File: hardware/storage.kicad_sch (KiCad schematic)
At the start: 15 parts, among them J6 Micro_SD_Card_Det1, U21 EMMC5.1_BGA153

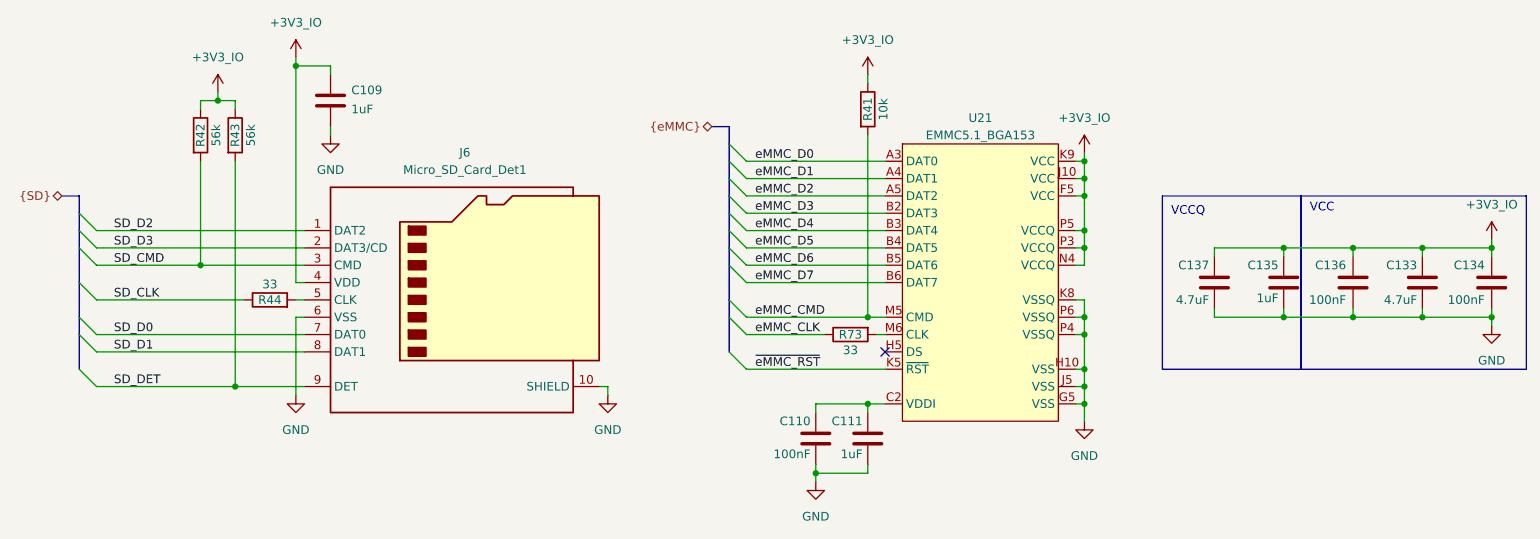
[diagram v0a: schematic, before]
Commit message: Update crystal
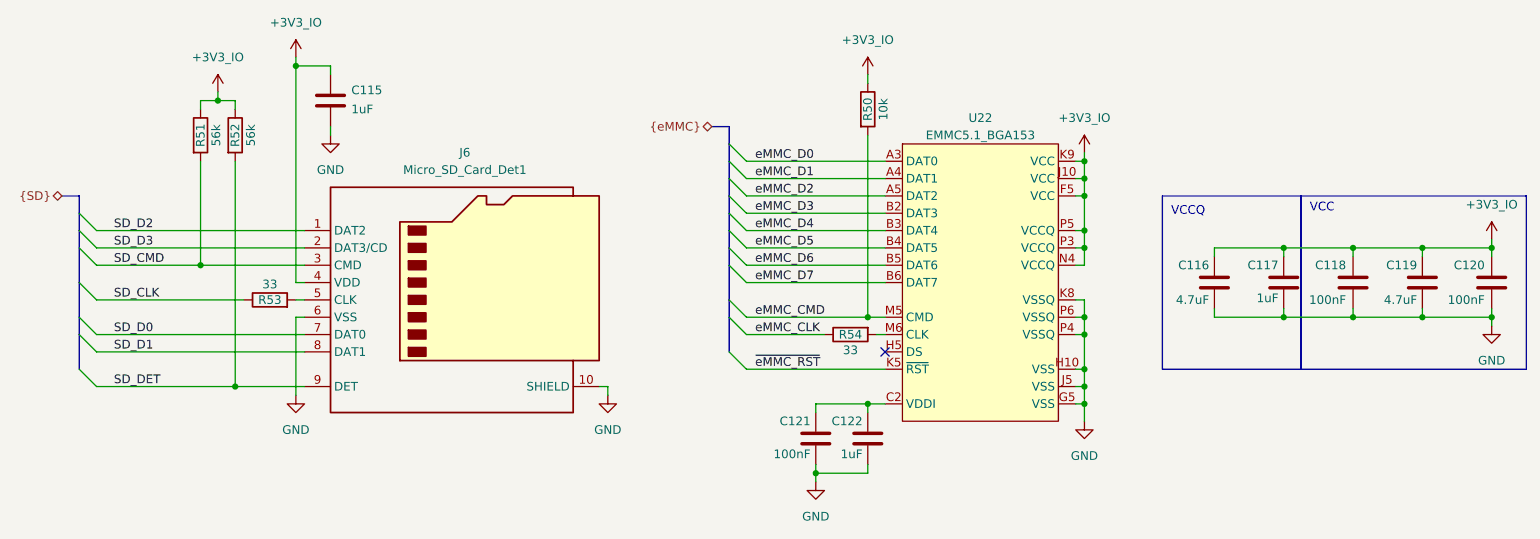
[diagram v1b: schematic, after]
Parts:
- renumbered C109 to C115, C137 to C116, C135 to C117, C136 to C118, C133 to C119, C134 to C120, C110 to C121, C111 to C122, R41 to R50, R42 to R51, R43 to R52, R44 to R53, R73 to R54, U21 to U22
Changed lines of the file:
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@@
 		(dnp no)
 		(fields_autoplaced yes)
-		(property "Reference" "#PWR0131"
+		(property "Reference" "#PWR0151"
 			(at 85.09 72.39 0)
 			(effects
@@
 			(project "cm0"
 				(path "/b53f5dbb-8078-4818-9e8f-fdf90ba6d854/bbbf0a3c-34ab-4b2d-85d9-faf7e9a88445"
-					(reference "#PWR0131")
+					(reference "#PWR0151")
 					(unit 1)
 				)
@@
 		(dnp no)
 		(fields_autoplaced yes)
-		(property "Reference" "#PWR0132"
+		(property "Reference" "#PWR0152"
 			(at 101.6 81.28 0)
 			(effects
@@
 			(project "cm0"
 				(path "/b53f5dbb-8078-4818-9e8f-fdf90ba6d854/bbbf0a3c-34ab-4b2d-85d9-faf7e9a88445"
-					(reference "#PWR0132")
+					(reference "#PWR0152")
 					(unit 1)
 				)
@@
 		(on_board yes)
 		(dnp no)
-		(property "Reference" "C111"
+		(property "Reference" "C122"
 			(at 179.578 116.84 0)
 			(effects
@@
 			(project "cm0"
 				(path "/b53f5dbb-8078-4818-9e8f-fdf90ba6d854/bbbf0a3c-34ab-4b2d-85d9-faf7e9a88445"
-					(reference "C111")
+					(reference "C122")
 					(unit 1)
 				)
@@
 		(on_board yes)
 		(dnp no)
-		(property "Reference" "R41"
+		(property "Reference" "R50"
 			(at 180.34 71.12 90)
 			(effects
@@
 			(project "cm0"
 				(path "/b53f5dbb-8078-4818-9e8f-fdf90ba6d854/bbbf0a3c-34ab-4b2d-85d9-faf7e9a88445"
-					(reference "R41")
+					(reference "R50")
 					(unit 1)
 				)
@@
 		(on_board yes)
 		(dnp no)
-		(property "Reference" "R42"
+		(property "Reference" "R51"
 			(at 82.55 74.93 90)
 			(effects
@@
 			(project "cm0"
 				(path "/b53f5dbb-8078-4818-9e8f-fdf90ba6d854/bbbf0a3c-34ab-4b2d-85d9-faf7e9a88445"
-					(reference "R42")
+					(reference "R51")
 					(unit 1)
 				)
@@
 		(on_board yes)
 		(dnp no)
-		(property "Reference" "C110"
+		(property "Reference" "C121"
 			(at 171.958 116.84 0)
 			(effects
@@
 			(project "cm0"
 				(path "/b53f5dbb-8078-4818-9e8f-fdf90ba6d854/bbbf0a3c-34ab-4b2d-85d9-faf7e9a88445"
-					(reference "C110")
+					(reference "C121")
 					(unit 1)
 				)
@@
 		(dnp no)
 		(fields_autoplaced yes)
-		(property "Reference" "#PWR0135"
+		(property "Reference" "#PWR0157"
 			(at 142.24 119.38 0)
 			(effects
@@
 			(project ""
 				(path "/b53f5dbb-8078-4818-9e8f-fdf90ba6d854/bbbf0a3c-34ab-4b2d-85d9-faf7e9a88445"
-					(reference "#PWR0135")
+					(reference "#PWR0157")
 					(unit 1)
 				)
@@
 		(on_board yes)
 		(dnp no)
-		(property "Reference" "C136"
+		(property "Reference" "C118"
 			(at 250.444 93.98 0)
 			(effects
@@
 			(project "cm0"
 				(path "/b53f5dbb-8078-4818-9e8f-fdf90ba6d854/bbbf0a3c-34ab-4b2d-85d9-faf7e9a88445"
-					(reference "C136")
+					(reference "C118")
 					(unit 1)
 				)
@@
 		(on_board yes)
 		(dnp no)
-		(property "Reference" "C134"
+		(property "Reference" "C120"
 			(at 270.764 93.98 0)
 			(effects
@@
 			(project "cm0"
 				(path "/b53f5dbb-8078-4818-9e8f-fdf90ba6d854/bbbf0a3c-34ab-4b2d-85d9-faf7e9a88445"
-					(reference "C134")
+					(reference "C120")
 					(unit 1)
 				)
@@
 		(dnp no)
 		(fields_autoplaced yes)
-		(property "Reference" "#PWR0134"
+		(property "Reference" "#PWR0156"
 			(at 96.52 119.38 0)
 			(effects
@@
 			(project ""
 				(path "/b53f5dbb-8078-4818-9e8f-fdf90ba6d854/bbbf0a3c-34ab-4b2d-85d9-faf7e9a88445"
-					(reference "#PWR0134")
+					(reference "#PWR0156")
 					(unit 1)
 				)
@@
 		(on_board yes)
 		(dnp no)
-		(property "Reference" "C137"
+		(property "Reference" "C116"
 			(at 230.378 93.98 0)
 			(effects
@@
 			(project "cm0"
 				(path "/b53f5dbb-8078-4818-9e8f-fdf90ba6d854/bbbf0a3c-34ab-4b2d-85d9-faf7e9a88445"
-					(reference "C137")
+					(reference "C116")
 					(unit 1)
 				)
@@
 		(dnp no)
 		(fields_autoplaced yes)
-		(property "Reference" "#PWR0129"
+		(property "Reference" "#PWR0149"
 			(at 96.52 67.31 0)
 			(effects
@@
 			(project ""
 				(path "/b53f5dbb-8078-4818-9e8f-fdf90ba6d854/bbbf0a3c-34ab-4b2d-85d9-faf7e9a88445"
-					(reference "#PWR0129")
+					(reference "#PWR0149")
 					(unit 1)
 				)
@@
 		(on_board yes)
 		(dnp no)
-		(property "Reference" "C135"
+		(property "Reference" "C117"
 			(at 240.538 93.98 0)
 			(effects
@@
 			(project "cm0"
 				(path "/b53f5dbb-8078-4818-9e8f-fdf90ba6d854/bbbf0a3c-34ab-4b2d-85d9-faf7e9a88445"
-					(reference "C135")
+					(reference "C117")
 					(unit 1)
 				)
@@
 		(on_board yes)
 		(dnp no)
-		(property "Reference" "R44"
+		(property "Reference" "R53"
 			(at 92.71 99.06 90)
 			(effects
@@
 			(project "cm0"
 				(path "/b53f5dbb-8078-4818-9e8f-fdf90ba6d854/bbbf0a3c-34ab-4b2d-85d9-faf7e9a88445"
-					(reference "R44")
+					(reference "R53")
 					(unit 1)
 				)
@@
 		(on_board yes)
 		(dnp no)
-		(property "Reference" "C133"
+		(property "Reference" "C119"
 			(at 260.858 93.98 0)
 			(effects
@@
 			(project "cm0"
 				(path "/b53f5dbb-8078-4818-9e8f-fdf90ba6d854/bbbf0a3c-34ab-4b2d-85d9-faf7e9a88445"
-					(reference "C133")
+					(reference "C119")
 					(unit 1)
 				)
@@
 		(dnp no)
 		(fields_autoplaced yes)
-		(property "Reference" "#PWR0187"
+		(property "Reference" "#PWR0154"
 			(at 271.78 93.98 0)
 			(effects
@@
 			(project "cm0"
 				(path "/b53f5dbb-8078-4818-9e8f-fdf90ba6d854/bbbf0a3c-34ab-4b2d-85d9-faf7e9a88445"
-					(reference "#PWR0187")
+					(reference "#PWR0154")
 					(unit 1)
 				)
@@
 		(dnp no)
 		(fields_autoplaced yes)
-		(property "Reference" "#PWR0136"
+		(property "Reference" "#PWR0158"
 			(at 212.09 123.19 0)
 			(effects
@@
 			(project "cm0"
 				(path "/b53f5dbb-8078-4818-9e8f-fdf90ba6d854/bbbf0a3c-34ab-4b2d-85d9-faf7e9a88445"
-					(reference "#PWR0136")
+					(reference "#PWR0158")
 					(unit 1)
 				)
@@
 		(dnp no)
 		(fields_autoplaced yes)
-		(property "Reference" "#PWR0176"
+		(property "Reference" "#PWR0153"
 			(at 212.09 81.28 0)
 			(effects
@@
 			(project "cm0"
 				(path "/b53f5dbb-8078-4818-9e8f-fdf90ba6d854/bbbf0a3c-34ab-4b2d-85d9-faf7e9a88445"
-					(reference "#PWR0176")
+					(reference "#PWR0153")
 					(unit 1)
 				)
@@
 		(dnp no)
 		(fields_autoplaced yes)
-		(property "Reference" "#PWR0137"
+		(property "Reference" "#PWR0159"
 			(at 172.72 132.08 0)
 			(effects
@@
 			(project ""
 				(path "/b53f5dbb-8078-4818-9e8f-fdf90ba6d854/bbbf0a3c-34ab-4b2d-85d9-faf7e9a88445"
-					(reference "#PWR0137")
+					(reference "#PWR0159")
 					(unit 1)
 				)
@@
 		(on_board yes)
 		(dnp no)
-		(property "Reference" "R43"
+		(property "Reference" "R52"
 			(at 87.63 74.93 90)
 			(effects
@@
 			(project "cm0"
 				(path "/b53f5dbb-8078-4818-9e8f-fdf90ba6d854/bbbf0a3c-34ab-4b2d-85d9-faf7e9a88445"
-					(reference "R43")
+					(reference "R52")
 					(unit 1)
 				)
@@
 		(dnp no)
 		(fields_autoplaced yes)
-		(property "Reference" "#PWR0130"
+		(property "Reference" "#PWR0150"
 			(at 180.34 69.85 0)
 			(effects
@@
 			(project "cm0"
 				(path "/b53f5dbb-8078-4818-9e8f-fdf90ba6d854/bbbf0a3c-34ab-4b2d-85d9-faf7e9a88445"
-					(reference "#PWR0130")
+					(reference "#PWR0150")
 					(unit 1)
 				)
@@
 		(dnp no)
 		(fields_autoplaced yes)
-		(property "Reference" "#PWR0186"
+		(property "Reference" "#PWR0155"
 			(at 271.78 109.22 0)
 			(effects
@@
 			(project "cm0"
 				(path "/b53f5dbb-8078-4818-9e8f-fdf90ba6d854/bbbf0a3c-34ab-4b2d-85d9-faf7e9a88445"
-					(reference "#PWR0186")
+					(reference "#PWR0155")
 					(unit 1)
 				)
@@
 		(dnp no)
 		(fields_autoplaced yes)
-		(property "Reference" "U21"
+		(property "Reference" "U22"
 			(at 196.85 72.39 0)
 			(effects
@@
 			(project ""
 				(path "/b53f5dbb-8078-4818-9e8f-fdf90ba6d854/bbbf0a3c-34ab-4b2d-85d9-faf7e9a88445"
-					(reference "U21")
+					(reference "U22")
 					(unit 1)
 				)
@@
 		(on_board yes)
 		(dnp no)
-		(property "Reference" "R73"
+		(property "Reference" "R54"
 			(at 177.8 104.14 90)
 			(effects
@@
 			(project "cm0"
 				(path "/b53f5dbb-8078-4818-9e8f-fdf90ba6d854/bbbf0a3c-34ab-4b2d-85d9-faf7e9a88445"
-					(reference "R73")
+					(reference "R54")
 					(unit 1)
 				)
@@
 		(on_board yes)
 		(dnp no)
-		(property "Reference" "C109"
+		(property "Reference" "C115"
 			(at 104.648 68.326 0)
 			(effects
@@
 			(project "cm0"
 				(path "/b53f5dbb-8078-4818-9e8f-fdf90ba6d854/bbbf0a3c-34ab-4b2d-85d9-faf7e9a88445"
-					(reference "C109")
-					(unit 1)
-				)
+					(reference "C115")
+					(unit 1)
+				)

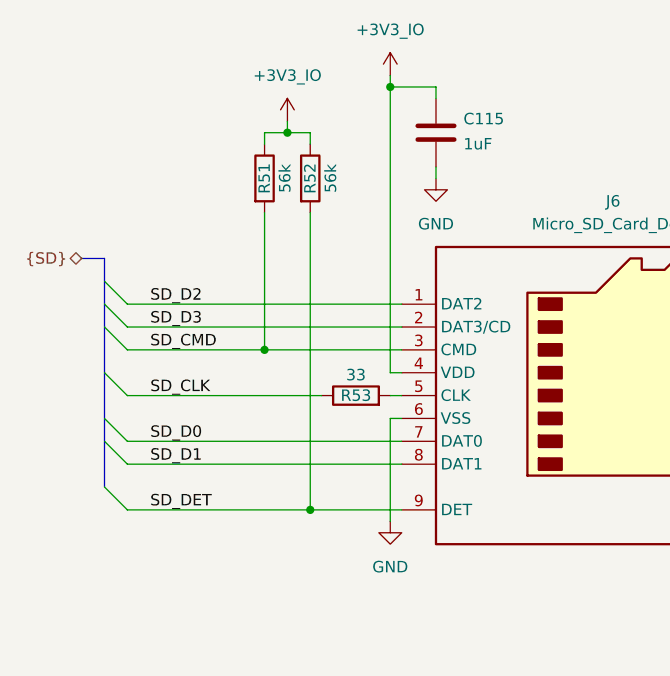
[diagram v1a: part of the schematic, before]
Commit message: Add schematic pdf
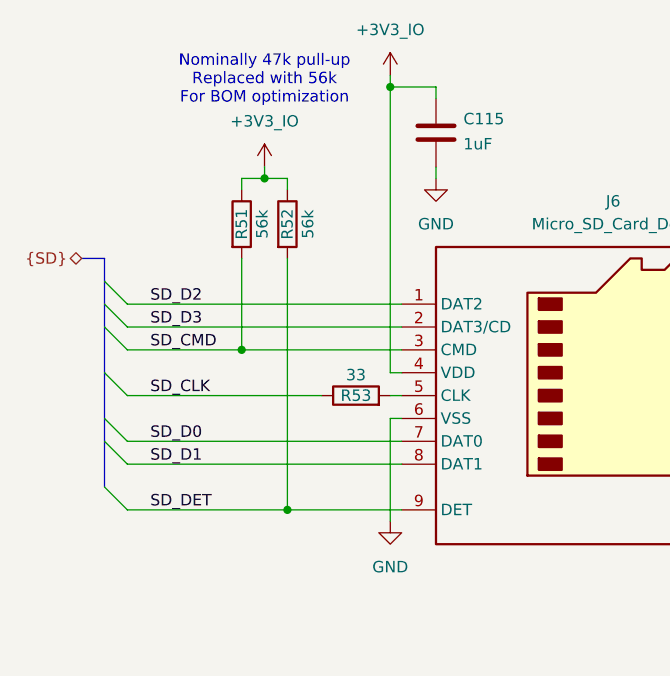
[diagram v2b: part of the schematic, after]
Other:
- note added: "Nominally 47k pull-up Replaced with 56k For BOM optimization"
- title: Icepi CM0 -> Icepi SBC
- moved on the sheet: R51, R52
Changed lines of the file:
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@@
 	(paper "A4")
 	(title_block
-		(title "Icepi CM0")
-		(date "2025-11-21")
+		(title "Icepi SBC")
+		(date "2025-12-21")
 		(rev "v1.0")
 		(company "Icy Electronics")
 		(comment 1 "Chengyin Yao (cheyao)")
-		(comment 2 "https://github.com/cheyao/icepi-cm0")
+		(comment 2 "https://github.com/cheyao/icepi-sbc")
 		(comment 3 "License: Solderpad")
 	)
@@
 		)
 	)
+	(text "Nominally 47k pull-up\nReplaced with 56k\nFor BOM optimization"
+		(exclude_from_sim no)
+		(at 82.55 64.008 0)
+		(effects
+			(font
+				(size 1.27 1.27)
+			)
+		)
+	)
 	(text "VCCQ"
 		(exclude_from_sim no)
@@
 	)
 	(junction
-		(at 87.63 111.76)
-		(diameter 0)
-		(color 0 0 0 0)
-	)
-	(junction
 		(at 251.46 91.44)
 		(diameter 0)
@@
 	)
 	(junction
+		(at 80.01 93.98)
+		(diameter 0)
+		(color 0 0 0 0)
+	)
+	(junction
 		(at 212.09 101.6)
 		(diameter 0)
@@
 	)
 	(junction
-		(at 85.09 69.85)
+		(at 82.55 74.93)
 		(diameter 0)
 		(color 0 0 0 0)
@@
 	)
 	(junction
-		(at 82.55 93.98)
-		(diameter 0)
-		(color 0 0 0 0)
-	)
-	(junction
 		(at 271.78 101.6)
 		(diameter 0)
@@
 	)
 	(junction
+		(at 85.09 111.76)
+		(diameter 0)
+		(color 0 0 0 0)
+	)
+	(junction
 		(at 271.78 91.44)
 		(diameter 0)
@@
 	(wire
 		(pts
-			(xy 85.09 68.58) (xy 85.09 69.85)
+			(xy 82.55 73.66) (xy 82.55 74.93)
 		)
 		(stroke
@@
 	(wire
 		(pts
-			(xy 87.63 111.76) (xy 97.79 111.76)
-		)
-		(stroke
-			(width 0)
-			(type default)
-		)
-	)
-	(wire
-		(pts
 			(xy 67.31 106.68) (xy 97.79 106.68)
 		)
@@
 		)
 	)
-	(wire
-		(pts
-			(xy 82.55 93.98) (xy 97.79 93.98)
-		)
-		(stroke
-			(width 0)
-			(type default)
-		)
-	)
 	(bus
 		(pts
@@
 	(wire
 		(pts
-			(xy 67.31 111.76) (xy 87.63 111.76)
+			(xy 67.31 111.76) (xy 85.09 111.76)
 		)
 		(stroke
@@
 	(wire
 		(pts
-			(xy 85.09 69.85) (xy 87.63 69.85)
+			(xy 82.55 74.93) (xy 85.09 74.93)
 		)
 		(stroke
@@
 	(wire
 		(pts
-			(xy 82.55 69.85) (xy 82.55 71.12)
+			(xy 80.01 74.93) (xy 80.01 76.2)
 		)
 		(stroke
@@
 	(wire
 		(pts
-			(xy 87.63 69.85) (xy 87.63 71.12)
+			(xy 85.09 74.93) (xy 85.09 76.2)
 		)
 		(stroke
@@
 	(wire
 		(pts
-			(xy 82.55 78.74) (xy 82.55 93.98)
+			(xy 80.01 83.82) (xy 80.01 93.98)
 		)
 		(stroke
@@
 	(wire
 		(pts
+			(xy 80.01 93.98) (xy 97.79 93.98)
+		)
+		(stroke
+			(width 0)
+			(type default)
+		)
+	)
+	(wire
+		(pts
 			(xy 67.31 99.06) (xy 88.9 99.06)
 		)
@@
 	(wire
 		(pts
-			(xy 67.31 93.98) (xy 82.55 93.98)
+			(xy 67.31 93.98) (xy 80.01 93.98)
 		)
 		(stroke
@@
 	(wire
 		(pts
-			(xy 85.09 69.85) (xy 82.55 69.85)
+			(xy 82.55 74.93) (xy 80.01 74.93)
 		)
 		(stroke
@@
 	(wire
 		(pts
-			(xy 87.63 78.74) (xy 87.63 111.76)
+			(xy 85.09 83.82) (xy 85.09 111.76)
+		)
+		(stroke
+			(width 0)
+			(type default)
+		)
+	)
+	(wire
+		(pts
+			(xy 85.09 111.76) (xy 97.79 111.76)
 		)
 		(stroke
@@
 	(symbol
 		(lib_id "cm0:+3V3_IO")
-		(at 85.09 68.58 0)
+		(at 82.55 73.66 0)
 		(unit 1)
 		(exclude_from_sim no)
@@
 		(fields_autoplaced yes)
 		(property "Reference" "#PWR0151"
-			(at 85.09 72.39 0)
+			(at 82.55 77.47 0)
 			(effects
 				(font
@@
 		)
 		(property "Value" "+3V3_IO"
-			(at 85.09 63.5 0)
+			(at 82.55 68.58 0)
 			(effects
 				(font
@@
 		)
 		(property "Footprint" ""
-			(at 85.09 68.58 0)
+			(at 82.55 73.66 0)
 			(effects
 				(font
@@
 		)
 		(property "Datasheet" ""
-			(at 85.09 68.58 0)
+			(at 82.55 73.66 0)
 			(effects
 				(font
@@
 		)
 		(property "Description" "Power symbol creates a global label with name \"+3V3_IO\""
-			(at 85.09 68.58 0)
+			(at 82.55 73.66 0)
 			(effects
 				(font
@@
 	(symbol
 		(lib_id "Device:R")
-		(at 82.55 74.93 0)
+		(at 80.01 80.01 0)
 		(unit 1)
 		(exclude_from_sim no)
@@
 		(dnp no)
 		(property "Reference" "R51"
-			(at 82.55 74.93 90)
+			(at 80.01 80.01 90)
 			(effects
 				(font
@@
 		)
 		(property "Value" "56k"
-			(at 84.836 74.93 90)
+			(at 82.296 80.01 90)
 			(effects
 				(font
@@
 		)
 		(property "Footprint" "Resistor_SMD:R_0402_1005Metric"
-			(at 80.772 74.93 90)
+			(at 78.232 80.01 90)
 			(effects
 				(font
@@
 		)
 		(property "Datasheet" "~"
-			(at 82.55 74.93 0)
+			(at 80.01 80.01 0)
 			(effects
 				(font
@@
 		)
 		(property "Description" "Resistor"
-			(at 82.55 74.93 0)
+			(at 80.01 80.01 0)
 			(effects
 				(font
@@
 		)
 		(property "LCSC Part #" "C25796"
-			(at 82.55 74.93 90)
+			(at 80.01 80.01 90)
 			(effects
 				(font
@@
 		)
 		(property "FT Position Offset" ""
-			(at 82.55 74.93 90)
+			(at 80.01 80.01 90)
 			(effects
 				(font
@@
 		)
 		(property "FT Rotation Offset" ""
-			(at 82.55 74.93 90)
+			(at 80.01 80.01 90)
 			(effects
 				(font
@@
 	(symbol
 		(lib_id "Device:R")
-		(at 87.63 74.93 0)
+		(at 85.09 80.01 0)
 		(unit 1)
 		(exclude_from_sim no)
@@
 		(dnp no)
 		(property "Reference" "R52"
-			(at 87.63 74.93 90)
+			(at 85.09 80.01 90)
 			(effects
 				(font
@@
 		)
 		(property "Value" "56k"
-			(at 89.916 74.93 90)
+			(at 87.376 80.01 90)
 			(effects
 				(font
@@
 		)
 		(property "Footprint" "Resistor_SMD:R_0402_1005Metric"
-			(at 85.852 74.93 90)
+			(at 83.312 80.01 90)
 			(effects
 				(font
@@
 		)
 		(property "Datasheet" "~"
-			(at 87.63 74.93 0)
+			(at 85.09 80.01 0)
 			(effects
 				(font
@@
 		)
 		(property "Description" "Resistor"
-			(at 87.63 74.93 0)
+			(at 85.09 80.01 0)
 			(effects
 				(font
@@
 		)
 		(property "LCSC Part #" "C25796"
-			(at 87.63 74.93 90)
+			(at 85.09 80.01 90)
 			(effects
 				(font
@@
 		)
 		(property "FT Position Offset" ""
-			(at 87.63 74.93 90)
+			(at 85.09 80.01 90)
 			(effects
 				(font
@@
 		)
 		(property "FT Rotation Offset" ""
-			(at 87.63 74.93 90)
+			(at 85.09 80.01 90)
 			(effects
 				(font
